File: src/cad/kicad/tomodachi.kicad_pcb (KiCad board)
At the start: 2 copper layers, 56 x 69.5 mm, 9 parts, among them U1 XIAO-ESP32-C3-DIP, U2 KY-040, U3 TC00500

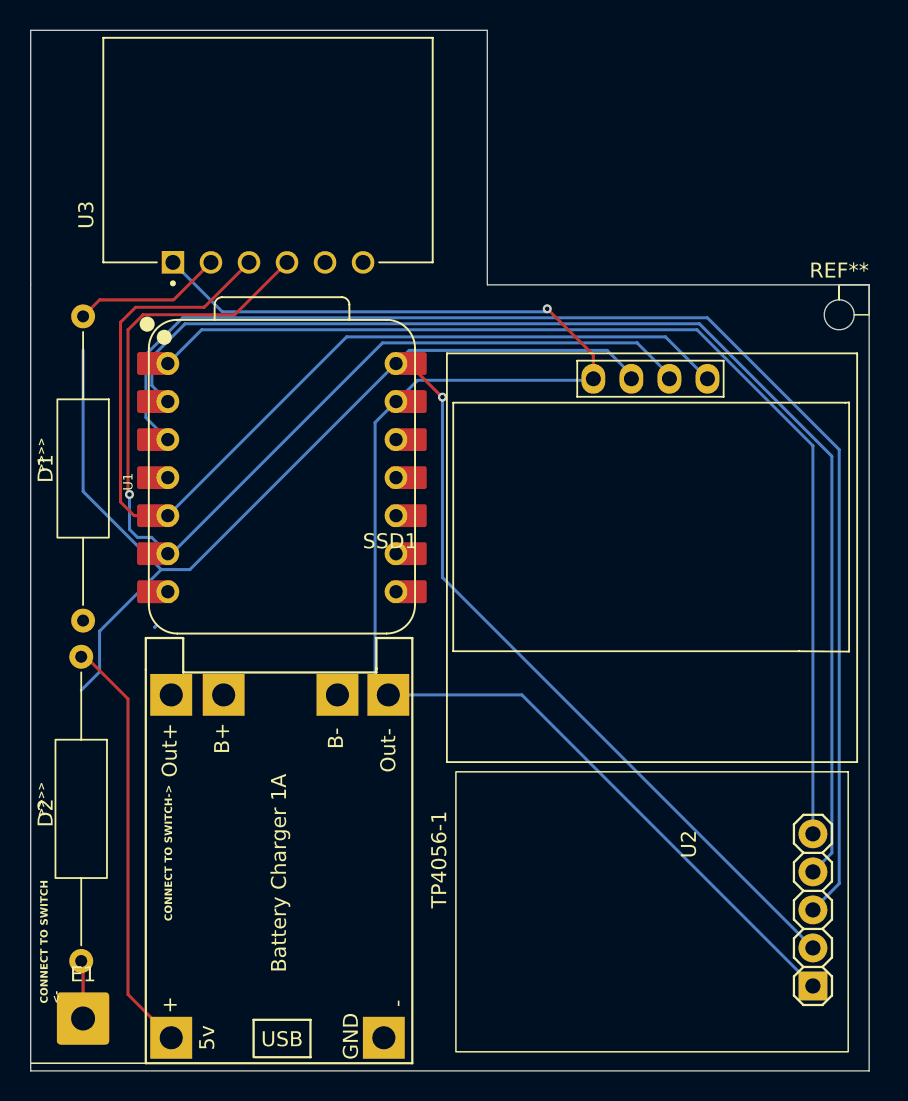
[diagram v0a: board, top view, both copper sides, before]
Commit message: fixed PCB & added BOM and 3D files
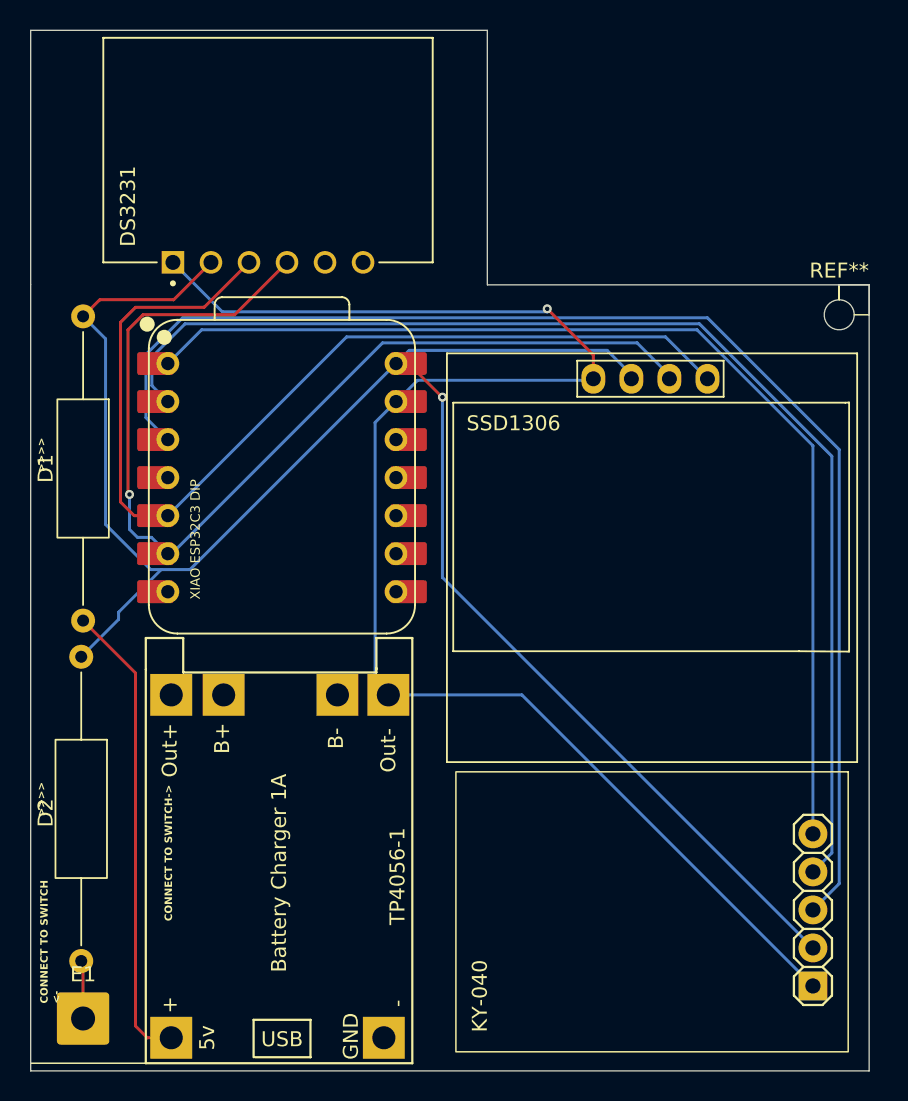
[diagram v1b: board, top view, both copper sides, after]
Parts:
- XIAO ESP32C3 DIP: renamed from U1
- renumbered U3 to DS3231, U2 to KY-040, SSD1 to SSD1306
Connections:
- DS3231 pad 6: Net-(D1-K) -> Net-(SSD1-GND)
- KY-040 pad GND: Net-(D1-K) -> Net-(SSD1-GND)
- SSD1306 pad 1: Net-(D1-K) -> Net-(SSD1-GND)
- TP4056-1 pad 4: Net-(D1-K) -> Net-(SSD1-GND)
- XIAO ESP32C3 DIP pad 13: Net-(D1-K) -> Net-(SSD1-GND)
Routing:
- net Net-(SSD1-GND): track 0.00 -> 103.3 mm, vias 0 -> 1
- net Net-(D1-K): track 229.4 -> 126.2 mm, vias 2 -> 1
- net Net-(D1-A): track 28.1 -> 31.2 mm
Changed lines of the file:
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@@
 			(outputformat 1)
 			(mirror no)
-			(drillshape 1)
+			(drillshape 0)
 			(scaleselection 1)
-			(outputdirectory "")
+			(outputdirectory "../gerbers/")
 		)
 	)
@@
 		(at 130.1875 121.9875 90)
 		(property "Reference" "TP4056-1"
-			(at 13.6 19.6 90)
+			(at 12.4875 16.8125 90)
 			(layer "F.SilkS")
 			(effects
@@
 			(layers "*.Cu" "*.Mask")
 			(remove_unused_layers no)
-			(net "Net-(D1-K)")
+			(net "Net-(SSD1-GND)")
 			(pinfunction "Out-_4")
 			(pintype "power_in")
@@
 		(layer "F.Cu")
 		(at 139.28 82.875 90)
-		(property "Reference" "U1"
-			(at -0.275 -10.275 90)
+		(property "Reference" "XIAO ESP32C3 DIP"
+			(at -4.125 -5.78 90)
 			(unlocked yes)
 			(layer "F.SilkS")
@@
 			(layers "*.Cu" "*.Mask")
 			(remove_unused_layers no)
-			(net "Net-(D1-K)")
+			(net "Net-(SSD1-GND)")
 			(pinfunction "GND_13")
 			(pintype "passive")
@@
 			(layers "F.Cu" "F.Mask")
 			(roundrect_rratio 0.1)
-			(net "Net-(D1-K)")
+			(net "Net-(SSD1-GND)")
 			(pinfunction "GND_13")
 			(pintype "passive")
@@
 		(layer "F.Cu")
 		(at 138.35 68.5 90)
-		(property "Reference" "U3"
-			(at 3.175 -12.135 90)
+		(property "Reference" "DS3231"
+			(at 3.75 -9.35 90)
 			(layer "F.SilkS")
 			(effects
@@
 		(sheetname "/")
 		(sheetfile "tomodachi.kicad_sch")
+		(units
+			(unit
+				(name "A")
+				(pins "3" "4" "5" "1" "2" "6")
+			)
+		)
 		(attr through_hole)
 		(duplicate_pad_numbers_are_jumpers no)
@@
 			(layers "*.Cu" "*.Mask")
 			(remove_unused_layers no)
-			(net "Net-(D1-K)")
+			(net "Net-(SSD1-GND)")
 			(pinfunction "GND_6")
 			(pintype "power_in")
@@
 		(layer "F.Cu")
 		(at 163.7 86.875)
-		(property "Reference" "SSD1"
-			(at -17.191072 0.254 0)
+		(property "Reference" "SSD1306"
+			(at -8.95 -7.625 0)
 			(layer "F.SilkS")
 			(effects
@@
 			(layers "*.Cu" "*.Mask")
 			(remove_unused_layers no)
-			(net "Net-(D1-K)")
+			(net "Net-(SSD1-GND)")
 			(pinfunction "GND_1")
 			(pintype "power_in")
@@
 		(at 164 111.875 -90)
 		(descr "<b>PIN HEADER</b>")
-		(property "Reference" "U2"
-			(at -4.5212 -2.4638 90)
+		(property "Reference" "KY-040"
+			(at 5.625 11.5 90)
 			(layer "F.SilkS")
 			(effects
@@
 			(layers "*.Cu" "*.Mask")
 			(remove_unused_layers no)
-			(net "Net-(D1-K)")
+			(net "Net-(SSD1-GND)")
 			(pinfunction "GND_GND")
 			(pintype "power_in")
@@
 	)
 	(segment
-		(start 129 97.66)
-		(end 126 94.66)
+		(start 129.5 119.5)
+		(end 129.5 95.925)
 		(width 0.2)
 		(layer "F.Cu")
@@
 	)
 	(segment
-		(start 129 117.4)
-		(end 129 97.66)
+		(start 129.5 95.925)
+		(end 126 92.425)
 		(width 0.2)
 		(layer "F.Cu")
@@
 	(segment
 		(start 131.8875 120.2875)
-		(end 129 117.4)
+		(end 130.2875 120.2875)
 		(width 0.2)
 		(layer "F.Cu")
@@
 	)
 	(segment
-		(start 150 77.5)
-		(end 149.98 77.5)
+		(start 130.2875 120.2875)
+		(end 129.5 119.5)
 		(width 0.2)
 		(layer "F.Cu")
-		(net "Net-(D1-K)")
+		(net "Net-(D1-A)")
 	)
 	(segment
-		(start 157 71.6)
-		(end 160.08 74.68)
+		(start 150 77.5)
+		(end 149.98 77.5)
 		(width 0.2)
 		(layer "F.Cu")
@@
 	)
 	(segment
-		(start 160.08 74.68)
-		(end 160.08 76.275)
-		(width 0.2)
-		(layer "F.Cu")
-		(net "Net-(D1-K)")
-	)
-	(segment
 		(start 132.04 71)
 		(end 127.105 71)
@@
 	)
 	(via
-		(at 157 71.6)
-		(size 0.6)
-		(drill 0.3)
-		(layers "F.Cu" "B.Cu")
-		(net "Net-(D1-K)")
-	)
-	(via
 		(at 150 77.5)
 		(size 0.6)
@@
 	)
 	(segment
-		(start 130.890947 92.765947)
-		(end 130.781894 92.875)
-		(width 0.2)
-		(layer "B.Cu")
-		(net "Net-(D1-K)")
-	)
-	(segment
-		(start 135.3 71.8)
-		(end 157 71.8)
-		(width 0.2)
-		(layer "B.Cu")
-		(net "Net-(D1-K)")
-	)
-	(segment
 		(start 174.746 114.2875)
 		(end 150 89.5415)
@@
 	)
 	(segment
-		(start 146.9 77.795)
-		(end 146.92 77.795)
-		(width 0.2)
-		(layer "B.Cu")
-		(net "Net-(D1-K)")
-	)
-	(segment
 		(start 150 89.5415)
 		(end 150 77.5)
@@
 	)
 	(segment
-		(start 157 71.8)
-		(end 157 71.6)
-		(width 0.2)
-		(layer "B.Cu")
-		(net "Net-(D1-K)")
-	)
-	(segment
-		(start 127.1 95.85)
-		(end 127.1 93.137105)
-		(width 0.2)
-		(layer "B.Cu")
-		(net "Net-(D1-K)")
-	)
-	(segment
-		(start 126 83.796895)
-		(end 131.220105 89.017)
+		(start 131.220105 89.017)
+		(end 130.517 89.017)
 		(width 0.2)
 		(layer "B.Cu")
@@
 	)
 	(segment
-		(start 145.5 96.5)
-		(end 145.5 79.195)
+		(start 127.5 86)
+		(end 127.5 73.605)
 		(width 0.2)
 		(layer "B.Cu")
@@
 	)
 	(segment
-		(start 132 68.5)
-		(end 135.3 71.8)
-		(width 0.2)
-		(layer "B.Cu")
-		(net "Net-(D1-K)")
-	)
-	(segment
-		(start 125.875 97.075)
-		(end 127.1 95.85)
+		(start 130.517 89.017)
+		(end 127.5 86)
 		(width 0.2)
 		(layer "B.Cu")
@@
 	)
 	(segment
-		(start 146.9 75.255)
-		(end 147.78 74.375)
-		(width 0.2)
-		(layer "B.Cu")
-		(net "Net-(D1-K)")
-	)
-	(segment
-		(start 126 74.34)
-		(end 126 83.796895)
-		(width 0.2)
-		(layer "B.Cu")
-		(net "Net-(D1-K)")
-	)
-	(segment
-		(start 159.98 76.375)
-		(end 160.08 76.275)
-		(width 0.2)
-		(layer "B.Cu")
-		(net "Net-(D1-K)")
-	)
-	(segment
-		(start 155.306 97.3875)
-		(end 174.746 116.8275)
-		(width 0.2)
-		(layer "B.Cu")
-		(net "Net-(D1-K)")
-	)
-	(segment
-		(start 146.3875 97.3875)
-		(end 155.306 97.3875)
+		(start 127.5 73.605)
+		(end 126 72.105)
 		(width 0.2)
 		(layer "B.Cu")
@@
 	)
 	(segment
-		(start 145.5 79.195)
-		(end 146.9 77.795)
+		(start 125.875 94.84)
+		(end 128.368552 92.346448)
 		(width 0.2)
 		(layer "B.Cu")
@@
 	)
 	(segment
-		(start 127.1 93.137105)
+		(start 128.368552 91.868552)
 		(end 131.220105 89.017)
 		(width 0.2)
@@
 	)
 	(segment
-		(start 146.92 77.795)
-		(end 148.34 76.375)
-		(width 0.2)
-		(layer "B.Cu")
-		(net "Net-(D1-K)")
-	)
-	(segment
-		(start 130.781895 92.875)
-		(end 130.890947 92.765947)
+		(start 146.9 75.255)
+		(end 147.78 74.375)
 		(width 0.2)
 		(layer "B.Cu")
@@
 	)
 	(segment
-		(start 148.34 76.375)
-		(end 159.98 76.375)
+		(start 128.368552 92.346448)
+		(end 128.368552 91.868552)
 		(width 0.2)
 		(layer "B.Cu")
@@
 	)
 	(segment
-		(start 146.3875 97.3875)
-		(end 145.5 96.5)
-		(width 0.2)
-		(layer "B.Cu")
-		(net "Net-(D1-K)")
-	)
-	(segment
 		(start 174.746 80.746)
 		(end 167 73)
@@
 		(net "Net-(D2-A)")
 	)
+	(segment
+		(start 157 71.6)
+		(end 160.08 74.68)
+		(width 0.2)
+		(layer "F.Cu")
+		(net "Net-(SSD1-GND)")
+	)
+	(segment
+		(start 160.08 74.68)
+		(end 160.08 76.275)
+		(width 0.2)
+		(layer "F.Cu")
+		(net "Net-(SSD1-GND)")
+	)
+	(via
+		(at 157 71.6)
+		(size 0.6)
+		(drill 0.3)
+		(layers "F.Cu" "B.Cu")
+		(net "Net-(SSD1-GND)")
+	)
+	(segment
+		(start 135.3 71.8)
+		(end 157 71.8)
+		(width 0.2)
+		(layer "B.Cu")
+		(net "Net-(SSD1-GND)")
+	)
+	(segment
+		(start 146.9 77.795)
+		(end 146.92 77.795)
+		(width 0.2)
+		(layer "B.Cu")
+		(net "Net-(SSD1-GND)")
+	)
+	(segment
+		(start 157 71.8)
+		(end 157 71.6)
+		(width 0.2)
+		(layer "B.Cu")
+		(net "Net-(SSD1-GND)")
+	)
+	(segment
+		(start 145.5 96.5)
+		(end 145.5 79.195)
+		(width 0.2)
+		(layer "B.Cu")
+		(net "Net-(SSD1-GND)")
+	)
+	(segment
+		(start 132 68.5)
+		(end 135.3 71.8)
+		(width 0.2)
+		(layer "B.Cu")
+		(net "Net-(SSD1-GND)")
+	)
+	(segment
+		(start 159.98 76.375)
+		(end 160.08 76.275)
+		(width 0.2)
+		(layer "B.Cu")
+		(net "Net-(SSD1-GND)")
+	)
+	(segment
+		(start 155.306 97.3875)
+		(end 174.746 116.8275)
+		(width 0.2)
+		(layer "B.Cu")
+		(net "Net-(SSD1-GND)")
+	)
+	(segment
+		(start 146.3875 97.3875)
+		(end 155.306 97.3875)
+		(width 0.2)
+		(layer "B.Cu")
+		(net "Net-(SSD1-GND)")
+	)
+	(segment
+		(start 145.5 79.195)
+		(end 146.9 77.795)
+		(width 0.2)
+		(layer "B.Cu")
+		(net "Net-(SSD1-GND)")
+	)
+	(segment
+		(start 146.92 77.795)
+		(end 148.34 76.375)
+		(width 0.2)
+		(layer "B.Cu")
+		(net "Net-(SSD1-GND)")
+	)
+	(segment
+		(start 148.34 76.375)
+		(end 159.98 76.375)
+		(width 0.2)
+		(layer "B.Cu")
+		(net "Net-(SSD1-GND)")
+	)
+	(segment
+		(start 146.3875 97.3875)
+		(end 145.5 96.5)
+		(width 0.2)
+		(layer "B.Cu")
+		(net "Net-(SSD1-GND)")
+	)
 	(embedded_fonts no)
